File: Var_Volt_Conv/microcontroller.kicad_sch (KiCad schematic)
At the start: 13 parts, among them J201 Conn_01x05, SW201 SW_Push, U201 STM32G030F6Px, Y201 16MHz

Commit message: Add Power, digital and analog grounds
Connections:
- net GND renamed GNDD

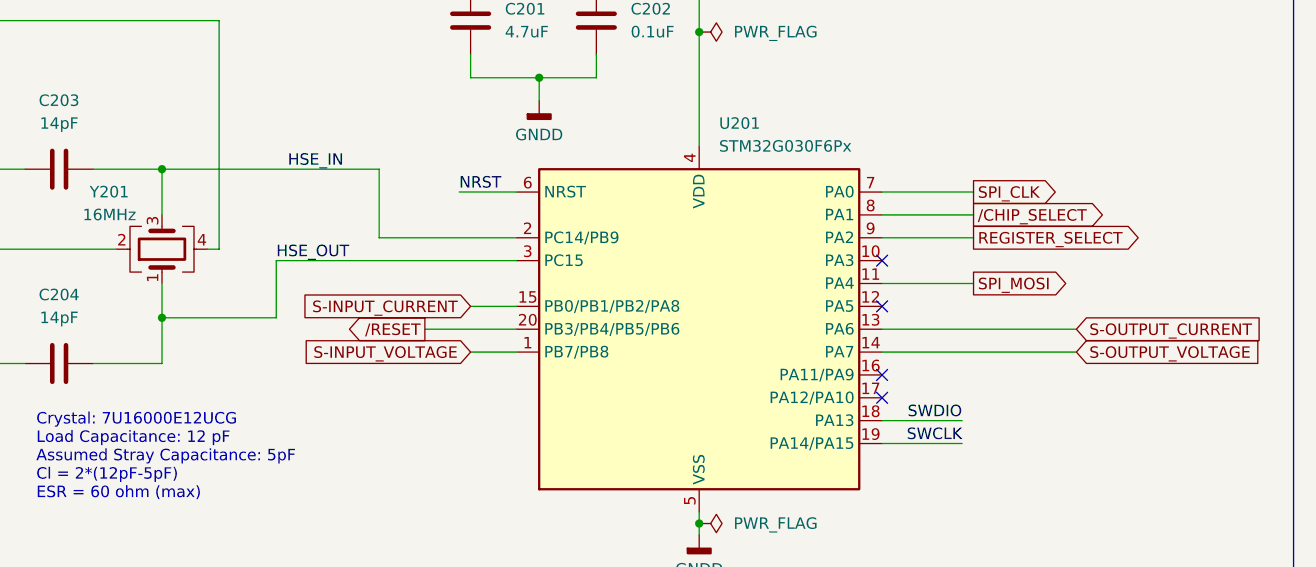
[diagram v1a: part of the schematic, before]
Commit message: Finish tracing all non-power related nets, changed uC pins for Chip Select, Register Select, Reset, Output Voltage sensing, input current sensing and output voltage sensing
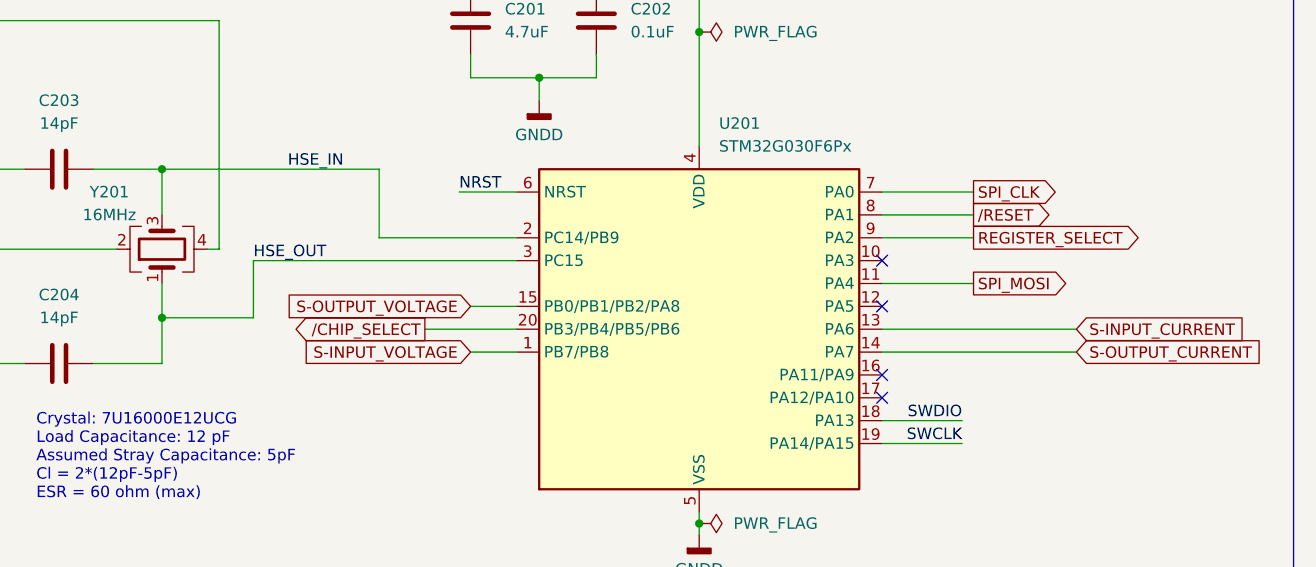
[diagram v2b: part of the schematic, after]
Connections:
- net S-INPUT_CURRENT: now also U201.13 (PA6); no longer U201.15 (PB0/PB1/PB2/PA8)
- net S-OUTPUT_CURRENT: now also U201.14 (PA7); no longer U201.13 (PA6)
- net S-OUTPUT_VOLTAGE: now also U201.15 (PB0/PB1/PB2/PA8); no longer U201.14 (PA7)
- net /CHIP_SELECT: now also U201.20 (PB3/PB4/PB5/PB6); no longer U201.8 (PA1)
- net /RESET: now also U201.8 (PA1); no longer U201.20 (PB3/PB4/PB5/PB6)
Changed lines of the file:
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@@
 	(wire
 		(pts
-			(xy 96.52 82.55) (xy 109.22 82.55)
+			(xy 96.52 82.55) (xy 106.68 82.55)
 		)
 		(stroke
@@
 	(wire
 		(pts
-			(xy 109.22 76.2) (xy 109.22 82.55)
+			(xy 106.68 76.2) (xy 106.68 82.55)
 		)
 		(stroke
@@
 	(wire
 		(pts
-			(xy 135.89 76.2) (xy 109.22 76.2)
+			(xy 135.89 76.2) (xy 106.68 76.2)
 		)
 		(stroke
@@
 	)
 	(label "HSE_OUT"
-		(at 109.22 76.2 0)
+		(at 106.68 76.2 0)
 		(fields_autoplaced yes)
 		(effects
@@
 			)
 			(justify right bottom)
-		)
-	)
-	(global_label "{slash}CHIP_SELECT"
-		(shape output)
-		(at 186.69 71.12 0)
-		(fields_autoplaced yes)
-		(effects
-			(font
-				(size 1.27 1.27)
-			)
-			(justify left)
-		)
-		(property "Intersheetrefs" "${INTERSHEET_REFS}"
-			(at 203.2218 71.12 0)
-			(effects
-				(font
-					(size 1.27 1.27)
-				)
-				(justify left)
-				(hide yes)
-			)
 		)
 	)
@@
 		)
 	)
-	(global_label "S-OUTPUT_VOLTAGE"
+	(global_label "{slash}CHIP_SELECT"
+		(shape output)
+		(at 125.73 83.82 180)
+		(fields_autoplaced yes)
+		(effects
+			(font
+				(size 1.27 1.27)
+			)
+			(justify right)
+		)
+		(property "Intersheetrefs" "${INTERSHEET_REFS}"
+			(at 109.1982 83.82 0)
+			(effects
+				(font
+					(size 1.27 1.27)
+				)
+				(justify right)
+				(hide yes)
+			)
+		)
+	)
+	(global_label "S-OUTPUT_CURRENT"
 		(shape input)
 		(at 198.12 86.36 0)
@@
 		)
 		(property "Intersheetrefs" "${INTERSHEET_REFS}"
-			(at 219.9738 86.36 0)
+			(at 220.639 86.36 0)
 			(effects
 				(font
@@
 		)
 	)
-	(global_label "S-OUTPUT_CURRENT"
+	(global_label "S-INPUT_CURRENT"
 		(shape input)
 		(at 198.12 83.82 0)
@@
 		)
 		(property "Intersheetrefs" "${INTERSHEET_REFS}"
-			(at 220.639 83.82 0)
+			(at 218.9457 83.82 0)
 			(effects
 				(font
@@
 				)
 				(justify left)
+				(hide yes)
+			)
+		)
+	)
+	(global_label "S-OUTPUT_VOLTAGE"
+		(shape input)
+		(at 130.81 81.28 180)
+		(fields_autoplaced yes)
+		(effects
+			(font
+				(size 1.27 1.27)
+			)
+			(justify right)
+		)
+		(property "Intersheetrefs" "${INTERSHEET_REFS}"
+			(at 108.9562 81.28 0)
+			(effects
+				(font
+					(size 1.27 1.27)
+				)
+				(justify right)
 				(hide yes)
 			)
@@
 		)
 	)
+	(global_label "{slash}RESET"
+		(shape output)
+		(at 186.69 71.12 0)
+		(fields_autoplaced yes)
+		(effects
+			(font
+				(size 1.27 1.27)
+			)
+			(justify left)
+		)
+		(property "Intersheetrefs" "${INTERSHEET_REFS}"
+			(at 196.7508 71.12 0)
+			(effects
+				(font
+					(size 1.27 1.27)
+				)
+				(justify left)
+				(hide yes)
+			)
+		)
+	)
+	(global_label "S-INPUT_VOLTAGE"
+		(shape input)
+		(at 130.81 86.36 180)
+		(fields_autoplaced yes)
+		(effects
+			(font
+				(size 1.27 1.27)
+			)
+			(justify right)
+		)
+		(property "Intersheetrefs" "${INTERSHEET_REFS}"
+			(at 110.6495 86.36 0)
+			(effects
+				(font
+					(size 1.27 1.27)
+				)
+				(justify right)
+				(hide yes)
+			)
+		)
+	)
 	(global_label "REGISTER_SELECT"
 		(shape output)
@@
 				(hide yes)
 			)
-		)
-	)
-	(global_label "{slash}RESET"
-		(shape output)
-		(at 125.73 83.82 180)
-		(fields_autoplaced yes)
-		(effects
-			(font
-				(size 1.27 1.27)
-			)
-			(justify right)
-		)
-		(property "Intersheetrefs" "${INTERSHEET_REFS}"
-			(at 115.6692 83.82 0)
-			(effects
-				(font
-					(size 1.27 1.27)
-				)
-				(justify right)
-				(hide yes)
-			)
-		)
-	)
-	(global_label "S-INPUT_VOLTAGE"
-		(shape input)
-		(at 130.81 86.36 180)
-		(fields_autoplaced yes)
-		(effects
-			(font
-				(size 1.27 1.27)
-			)
-			(justify right)
-		)
-		(property "Intersheetrefs" "${INTERSHEET_REFS}"
-			(at 110.6495 86.36 0)
-			(effects
-				(font
-					(size 1.27 1.27)
-				)
-				(justify right)
-				(hide yes)
-			)
-		)
-	)
-	(global_label "S-INPUT_CURRENT"
-		(shape input)
-		(at 130.81 81.28 180)
-		(fields_autoplaced yes)
-		(effects
-			(font
-				(size 1.27 1.27)
-			)
-			(justify right)
-		)
-		(property "Intersheetrefs" "${INTERSHEET_REFS}"
-			(at 109.9843 81.28 0)
-			(effects
-				(font
-					(size 1.27 1.27)
-				)
-				(justify right)
-				(hide yes)
-			)

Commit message: Labeled subcircuits in PCB
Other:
- title: (none) -> Variable Voltage Controller
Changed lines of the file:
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@@
 	(generator_version "8.0")
 	(paper "A4")
+	(title_block
+		(title "Variable Voltage Controller")
+		(date "2025-02-02")
+		(rev "1.0")
+	)
 	(junction
 		(at 96.52 82.55)

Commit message: Completed the BOM
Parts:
- C201: JLCPCB Part # (none) -> C76995; Manufacturer Part # (none) -> GRM155R60J475KE96D
- C202, C205: JLCPCB Part # (none) -> C155422; Manufacturer Part # (none) -> CL05B104KA5NNNC
- C203, C204: JLCPCB Part # (none) -> C458857; Manufacturer Part # (none) -> 0402N140J500CT
- D201, D202, D203, D204: JLCPCB Part # (none) -> C51450; Manufacturer Part # (none) -> PESD3V3L1BA,115
- J201: Manufacturer Part # (none) -> PPTC051LFBN-RC
- SW201: JLCPCB Part # (none) -> C2689642; Manufacturer Part # (none) -> PTS636SK25SMTRLFS
- U201: JLCPCB Part # (none) -> C724040; Manufacturer Part # (none) -> STM32G030F6P6
- Y201: JLCPCB Part # (none) -> C251610; Manufacturer Part # (none) -> 7U16000E12UCG
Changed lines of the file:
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@@
+			)
+		)
+		(property "JLCPCB Part #" "C2689642"
+			(at 59.69 148.59 0)
+			(effects
+				(font
+					(size 1.27 1.27)
+				)
+				(hide yes)
+			)
+		)
+		(property "Manufacturer Part #" "PTS636SK25SMTRLFS"
+			(at 59.69 148.59 0)
+			(effects
+				(font
+					(size 1.27 1.27)
+				)
+				(hide yes)
 			)
 		)
@@
 			)
 		)
+		(property "JLCPCB Part #" "C76995"
+			(at 130.81 49.53 0)
+			(effects
+				(font
+					(size 1.27 1.27)
+				)
+				(hide yes)
+			)
+		)
+		(property "Manufacturer Part #" "GRM155R60J475KE96D"
+			(at 130.81 49.53 0)
+			(effects
+				(font
+					(size 1.27 1.27)
+				)
+				(hide yes)
+			)
+		)
 		(pin "2"
 		)
@@
 			)
 		)
+		(property "JLCPCB Part #" "C51450"
+			(at 162.56 162.56 0)
+			(effects
+				(font
+					(size 1.27 1.27)
+				)
+				(hide yes)
+			)
+		)
+		(property "Manufacturer Part #" "PESD3V3L1BA,115"
+			(at 162.56 162.56 0)
+			(effects
+				(font
+					(size 1.27 1.27)
+				)
+				(hide yes)
+			)
+		)
 		(pin "1"
 		)
@@
 			)
 		)
+		(property "JLCPCB Part #" "C458857"
+			(at 85.09 66.04 0)
+			(effects
+				(font
+					(size 1.27 1.27)
+				)
+				(hide yes)
+			)
+		)
+		(property "Manufacturer Part #" "0402N140J500CT"
+			(at 85.09 66.04 0)
+			(effects
+				(font
+					(size 1.27 1.27)
+				)
+				(hide yes)
+			)
+		)
 		(pin "2"
 		)
@@
 			)
 		)
+		(property "JLCPCB Part #" "C251610"
+			(at 96.52 74.93 0)
+			(effects
+				(font
+					(size 1.27 1.27)
+				)
+				(hide yes)
+			)
+		)
+		(property "Manufacturer Part #" "7U16000E12UCG"
+			(at 96.52 74.93 0)
+			(effects
+				(font
+					(size 1.27 1.27)
+				)
+				(hide yes)
+			)
+		)
 		(pin "1"
 		)
@@
 			)
 		)
+		(property "JLCPCB Part #" "C51450"
+			(at 134.62 162.56 0)
+			(effects
+				(font
+					(size 1.27 1.27)
+				)
+				(hide yes)
+			)
+		)
+		(property "Manufacturer Part #" "PESD3V3L1BA,115"
+			(at 134.62 162.56 0)
+			(effects
+				(font
+					(size 1.27 1.27)
+				)
+				(hide yes)
+			)
+		)
 		(pin "1"
 		)
@@
 		)
 		(property "Description" "Unpolarized capacitor"
+			(at 85.09 87.63 0)
+			(effects
+				(font
+					(size 1.27 1.27)
+				)
+				(hide yes)
+			)
+		)
+		(property "JLCPCB Part #" "C458857"
+			(at 85.09 87.63 0)
+			(effects
+				(font
+					(size 1.27 1.27)
+				)
+				(hide yes)
+			)
+		)
+		(property "Manufacturer Part #" "0402N140J500CT"
 			(at 85.09 87.63 0)
 			(effects
@@
 			)
 		)
+		(property "JLCPCB Part #" ""
+			(at 104.14 147.32 0)
+			(effects
+				(font
+					(size 1.27 1.27)
+				)
+				(hide yes)
+			)
+		)
+		(property "Manufacturer Part #" "PPTC051LFBN-RC"
+			(at 104.14 147.32 0)
+			(effects
+				(font
+					(size 1.27 1.27)
+				)
+				(hide yes)
+			)
+		)
 		(pin "1"
 		)
@@
 			)
 		)
+		(property "JLCPCB Part #" "C51450"
+			(at 148.59 162.56 0)
+			(effects
+				(font
+					(size 1.27 1.27)
+				)
+				(hide yes)
+			)
+		)
+		(property "Manufacturer Part #" "PESD3V3L1BA,115"
+			(at 148.59 162.56 0)
+			(effects
+				(font
+					(size 1.27 1.27)
+				)
+				(hide yes)
+			)
+		)
 		(pin "1"
 		)
@@
 			)
 		)
+		(property "JLCPCB Part #" "C51450"
+			(at 120.65 162.56 0)
+			(effects
+				(font
+					(size 1.27 1.27)
+				)
+				(hide yes)
+			)
+		)
+		(property "Manufacturer Part #" "PESD3V3L1BA,115"
+			(at 120.65 162.56 0)
+			(effects
+				(font
+					(size 1.27 1.27)
+				)
+				(hide yes)
+			)
+		)
 		(pin "1"
 		)
@@
 			)
 		)
+		(property "JLCPCB Part #" "C155422"
+			(at 144.78 49.53 0)
+			(effects
+				(font
+					(size 1.27 1.27)
+				)
+				(hide yes)
+			)
+		)
+		(property "Manufacturer Part #" "CL05B104KA5NNNC"
+			(at 144.78 49.53 0)
+			(effects
+				(font
+					(size 1.27 1.27)
+				)
+				(hide yes)
+			)
+		)
 		(pin "2"
 		)
@@
 			)
 		)
+		(property "JLCPCB Part #" "C724040"
+			(at 156.21 83.82 0)
+			(effects
+				(font
+					(size 1.27 1.27)
+				)
+				(hide yes)
+			)
+		)
+		(property "Manufacturer Part #" "STM32G030F6P6"
+			(at 156.21 83.82 0)
+			(effects
+				(font
+					(size 1.27 1.27)
+				)
+				(hide yes)
+			)
+		)
 		(pin "1"
 		)
@@
 			(at 72.39 148.59 0)
 			(effects
+				(font
+					(size 1.27 1.27)
+				)
+				(hide yes)
+			)
+		)
+		(property "JLCPCB Part #" "C155422"
+			(at 72.39 148.59 0)
+			(effects
+				(font
+					(size 1.27 1.27)
+				)
+				(hide yes)
+			)
+		)
+		(property "Manufacturer Part #" "CL05B104KA5NNNC"
+			(at 72.39 148.59 0)
+			(effects

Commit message: Updated schematic, C121, R112 and SW201 now use components that are still in stock on JLCPCB
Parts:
- C201: JLCPCB Part # C76995 -> (none); LCSC (none) -> C76995
- C202, C205: JLCPCB Part # C155422 -> (none); LCSC (none) -> C155422
- C203, C204: JLCPCB Part # C458857 -> (none); LCSC (none) -> C458857
- D201, D202, D203, D204: JLCPCB Part # C51450 -> (none); LCSC (none) -> C51450
- SW201: JLCPCB Part # C2689642 -> (none); LCSC (none) -> C2689642; Manufacturer Part # PTS636SK25SMTRLFS -> GT-TC060B-H025-L1
- U201: JLCPCB Part # C724040 -> (none); LCSC (none) -> C724040
- Y201: JLCPCB Part # C251610 -> (none); LCSC (none) -> C251610
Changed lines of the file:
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@@
 			)
 		)
-		(property "JLCPCB Part #" "C2689642"
+		(property "Manufacturer Part #" "GT-TC060B-H025-L1"
 			(at 59.69 148.59 0)
 			(effects
@@
 			)
 		)
-		(property "Manufacturer Part #" "PTS636SK25SMTRLFS"
+		(property "LCSC" "C2689642"
 			(at 59.69 148.59 0)
 			(effects
@@
 			)
 		)
-		(property "JLCPCB Part #" "C76995"
-			(at 130.81 49.53 0)
-			(effects
-				(font
-					(size 1.27 1.27)
-				)
-				(hide yes)
-			)
-		)
 		(property "Manufacturer Part #" "GRM155R60J475KE96D"
 			(at 130.81 49.53 0)
@@
 			)
 		)
+		(property "LCSC" "C76995"
+			(at 130.81 49.53 0)
+			(effects
+				(font
+					(size 1.27 1.27)
+				)
+				(hide yes)
+			)
+		)
 		(pin "2"
 		)
@@
 			)
 		)
-		(property "JLCPCB Part #" "C51450"
-			(at 162.56 162.56 0)
-			(effects
-				(font
-					(size 1.27 1.27)
-				)
-				(hide yes)
-			)
-		)
 		(property "Manufacturer Part #" "PESD3V3L1BA,115"
 			(at 162.56 162.56 0)
@@
 			)
 		)
+		(property "LCSC" "C51450"
+			(at 162.56 162.56 0)
+			(effects
+				(font
+					(size 1.27 1.27)
+				)
+				(hide yes)
+			)
+		)
 		(pin "1"
 		)
@@
 			)
 		)
-		(property "JLCPCB Part #" "C458857"
-			(at 85.09 66.04 0)
-			(effects
-				(font
-					(size 1.27 1.27)
-				)
-				(hide yes)
-			)
-		)
 		(property "Manufacturer Part #" "0402N140J500CT"
 			(at 85.09 66.04 0)
@@
 			)
 		)
+		(property "LCSC" "C458857"
+			(at 85.09 66.04 0)
+			(effects
+				(font
+					(size 1.27 1.27)
+				)
+				(hide yes)
+			)
+		)
 		(pin "2"
 		)
@@
 			)
 		)
-		(property "JLCPCB Part #" "C251610"
-			(at 96.52 74.93 0)
-			(effects
-				(font
-					(size 1.27 1.27)
-				)
-				(hide yes)
-			)
-		)
 		(property "Manufacturer Part #" "7U16000E12UCG"
 			(at 96.52 74.93 0)
@@
 			)
 		)
+		(property "LCSC" "C251610"
+			(at 96.52 74.93 0)
+			(effects
+				(font
+					(size 1.27 1.27)
+				)
+				(hide yes)
+			)
+		)
 		(pin "1"
 		)
@@
 			)
 		)
-		(property "JLCPCB Part #" "C51450"
-			(at 134.62 162.56 0)
-			(effects
-				(font
-					(size 1.27 1.27)
-				)
-				(hide yes)
-			)
-		)
 		(property "Manufacturer Part #" "PESD3V3L1BA,115"
 			(at 134.62 162.56 0)
@@
 			)
 		)
+		(property "LCSC" "C51450"
+			(at 134.62 162.56 0)
+			(effects
+				(font
+					(size 1.27 1.27)
+				)
+				(hide yes)
+			)
+		)
 		(pin "1"
 		)
@@
 			)
 		)
-		(property "JLCPCB Part #" "C458857"
+		(property "Manufacturer Part #" "0402N140J500CT"
 			(at 85.09 87.63 0)
 			(effects
@@
 			)
 		)
-		(property "Manufacturer Part #" "0402N140J500CT"
+		(property "LCSC" "C458857"
 			(at 85.09 87.63 0)
 			(effects
@@
 			)
 		)
-		(property "JLCPCB Part #" ""
-			(at 104.14 147.32 0)
-			(effects
-				(font
-					(size 1.27 1.27)
-				)
-				(hide yes)
-			)
-		)
 		(property "Manufacturer Part #" "PPTC051LFBN-RC"
 			(at 104.14 147.32 0)
@@
 			)
 		)
-		(property "JLCPCB Part #" "C51450"
-			(at 148.59 162.56 0)
-			(effects
-				(font
-					(size 1.27 1.27)
-				)
-				(hide yes)
-			)
-		)
 		(property "Manufacturer Part #" "PESD3V3L1BA,115"
 			(at 148.59 162.56 0)
@@
 			)
 		)
+		(property "LCSC" "C51450"
+			(at 148.59 162.56 0)
+			(effects
+				(font
+					(size 1.27 1.27)
+				)
+				(hide yes)
+			)
+		)
 		(pin "1"
 		)
@@
 			)
 		)
-		(property "JLCPCB Part #" "C51450"
-			(at 120.65 162.56 0)
-			(effects
-				(font
-					(size 1.27 1.27)
-				)
-				(hide yes)
-			)
-		)
 		(property "Manufacturer Part #" "PESD3V3L1BA,115"
 			(at 120.65 162.56 0)
@@
 			)
 		)
+		(property "LCSC" "C51450"
+			(at 120.65 162.56 0)
+			(effects
+				(font
+					(size 1.27 1.27)
+				)
+				(hide yes)
+			)
+		)
 		(pin "1"
 		)
@@
 			)
 		)
-		(property "JLCPCB Part #" "C155422"
-			(at 144.78 49.53 0)
-			(effects
-				(font
-					(size 1.27 1.27)
-				)
-				(hide yes)
-			)
-		)
 		(property "Manufacturer Part #" "CL05B104KA5NNNC"
 			(at 144.78 49.53 0)
@@
 			)
 		)
+		(property "LCSC" "C155422"
+			(at 144.78 49.53 0)
+			(effects
+				(font
+					(size 1.27 1.27)
+				)
+				(hide yes)
+			)
+		)
 		(pin "2"
 		)
@@
 			)
 		)
-		(property "JLCPCB Part #" "C724040"
-			(at 156.21 83.82 0)
-			(effects
-				(font
-					(size 1.27 1.27)
-				)
-				(hide yes)
-			)
-		)
 		(property "Manufacturer Part #" "STM32G030F6P6"
 			(at 156.21 83.82 0)
@@
 			)
 		)
+		(property "LCSC" "C724040"
+			(at 156.21 83.82 0)
+			(effects
+				(font
+					(size 1.27 1.27)
+				)
+				(hide yes)
+			)
+		)
 		(pin "1"
 		)
@@
 			)
 		)
-		(property "JLCPCB Part #" "C155422"
-			(at 72.39 148.59 0)
-			(effects
-				(font
-					(size 1.27 1.27)
-				)
-				(hide yes)
-			)
-		)
 		(property "Manufacturer Part #" "CL05B104KA5NNNC"
 			(at 72.39 148.59 0)
 			(effects
+				(font
+					(size 1.27 1.27)
+				)
+				(hide yes)
+			)
+		)
+		(property "LCSC" "C155422"
+			(at 72.39 148.59 0)
+			(effects

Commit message: Update JLCPCB Production files
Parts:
- SW201: LCSC C2689642 -> C778169
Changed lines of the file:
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@@
 			)
 		)
-		(property "LCSC" "C2689642"
+		(property "LCSC" "C778169"
 			(at 59.69 148.59 0)
 			(effects

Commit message: Confirmed all basic components
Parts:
- C201: LCSC C76995 -> (none); Manufacturer Part # GRM155R60J475KE96D -> CL05A475MP5NRNC; lcsc (none) -> C23733
- C202, C205: LCSC C155422 -> (none); lcsc (none) -> C155422
- C203, C204: LCSC C458857 -> (none); lcsc (none) -> C458857
- D201, D202, D203, D204: LCSC C51450 -> (none); lcsc (none) -> C51450
- SW201: LCSC C778169 -> (none); lcsc (none) -> C778169
- U201: LCSC C724040 -> (none); lcsc (none) -> C724040
- Y201: LCSC C251610 -> (none); lcsc (none) -> C251610
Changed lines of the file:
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@@
 			)
 		)
-		(property "LCSC" "C778169"
+		(property "lcsc" "C778169"
 			(at 59.69 148.59 0)
 			(effects
@@
 			)
 		)
-		(property "Manufacturer Part #" "GRM155R60J475KE96D"
+		(property "Manufacturer Part #" "CL05A475MP5NRNC"
 			(at 130.81 49.53 0)
 			(effects
@@
 			)
 		)
-		(property "LCSC" "C76995"
+		(property "lcsc" "C23733"
 			(at 130.81 49.53 0)
 			(effects
@@
 			)
 		)
-		(property "LCSC" "C51450"
+		(property "lcsc" "C51450"
 			(at 162.56 162.56 0)
 			(effects
@@
 			)
 		)
-		(property "LCSC" "C458857"
+		(property "lcsc" "C458857"
 			(at 85.09 66.04 0)
 			(effects
@@
 			)
 		)
-		(property "LCSC" "C251610"
+		(property "lcsc" "C251610"
 			(at 96.52 74.93 0)
 			(effects
@@
 			)
 		)
-		(property "LCSC" "C51450"
+		(property "lcsc" "C51450"
 			(at 134.62 162.56 0)
 			(effects
@@
 			)
 		)
-		(property "LCSC" "C458857"
+		(property "lcsc" "C458857"
 			(at 85.09 87.63 0)
 			(effects
@@
 			)
 		)
-		(property "LCSC" "C51450"
+		(property "lcsc" "C51450"
 			(at 148.59 162.56 0)
 			(effects
@@
 			)
 		)
-		(property "LCSC" "C51450"
+		(property "lcsc" "C51450"
 			(at 120.65 162.56 0)
 			(effects
@@
 			)
 		)
-		(property "LCSC" "C155422"
+		(property "lcsc" "C155422"
 			(at 144.78 49.53 0)
 			(effects
@@
 			)
 		)
-		(property "LCSC" "C724040"
+		(property "lcsc" "C724040"
 			(at 156.21 83.82 0)
 			(effects
@@
 			)
 		)
-		(property "LCSC" "C155422"
+		(property "lcsc" "C155422"
 			(at 72.39 148.59 0)
 			(effects

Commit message: Will source switch from Digikey, decided what to source from digikey and what to source from JLCPCB
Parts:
- SW201: Manufacturer Part # GT-TC060B-H025-L1 -> PTS636SKG25SMTR LFS; lcsc C778169 -> (none)
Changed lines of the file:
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@@
 			)
 		)
-		(property "Manufacturer Part #" "GT-TC060B-H025-L1"
+		(property "Manufacturer Part #" "PTS636SKG25SMTR LFS"
 			(at 59.69 148.59 0)
 			(effects
@@
 			)
 		)
-		(property "lcsc" "C778169"
+		(property "lcsc" ""
 			(at 59.69 148.59 0)
 			(effects
